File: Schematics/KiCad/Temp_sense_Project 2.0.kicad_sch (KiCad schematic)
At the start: 0 parts

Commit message: Fix all errors and warnings
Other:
- sheet Power renamed Power and Isolation
- sheet mux side left renamed Multiplexers
- sheet MCU ports: added CAN RX, CAN TX, Fault Line 1; removed 5V GND, 5V PWR, Fault line 1, RXD, TXD
- sheet Power and Isolation ports: added none; removed 5V GND, 5V PWR
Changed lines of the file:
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@@
-	(wire
-		(pts
-			(xy 416.56 278.13) (xy 416.56 266.7)
-		)
-		(stroke
-			(width 0)
-			(type default)
-		)
-	)
 	(wire
 		(pts
@@
 		(pts
 			(xy 424.18 219.71) (xy 419.1 219.71)
-		)
-		(stroke
-			(width 0)
-			(type default)
-		)
-	)
-	(wire
-		(pts
-			(xy 419.1 278.13) (xy 419.1 266.7)
 		)
 		(stroke
@@
 			(color 128 255 128 1.0000)
 		)
-		(property "Sheetname" "mux side left"
+		(property "Sheetname" "Multiplexers"
 			(at 384.81 207.01 0)
 			(effects
@@
 			)
 		)
-		(pin "5V GND" input
-			(at 416.56 266.7 270)
-			(effects
-				(font
-					(size 1.27 1.27)
-				)
-				(justify left)
-			)
-		)
-		(pin "5V PWR" input
-			(at 419.1 266.7 270)
-			(effects
-				(font
-					(size 1.27 1.27)
-				)
-				(justify left)
-			)
-		)
-		(pin "TXD" output
+		(pin "Fault Line 1" output
+			(at 425.45 266.7 270)
+			(effects
+				(font
+					(size 1.27 1.27)
+				)
+				(justify left)
+			)
+		)
+		(pin "CAN RX" input
+			(at 378.46 266.7 270)
+			(effects
+				(font
+					(size 1.27 1.27)
+				)
+				(justify left)
+			)
+		)
+		(pin "CAN TX" output
 			(at 383.54 266.7 270)
-			(effects
-				(font
-					(size 1.27 1.27)
-				)
-				(justify left)
-			)
-		)
-		(pin "RXD" input
-			(at 378.46 266.7 270)
-			(effects
-				(font
-					(size 1.27 1.27)
-				)
-				(justify left)
-			)
-		)
-		(pin "Fault line 1" output
-			(at 425.45 266.7 270)
 			(effects
 				(font
@@
 			(color 128 255 128 1.0000)
 		)
-		(property "Sheetname" "Power"
+		(property "Sheetname" "Power and Isolation"
 			(at 371.3984 298.45 90)
 			(effects
@@
 			)
 		)
-		(pin "5V GND" output
-			(at 416.56 278.13 90)
-			(effects
-				(font
-					(size 1.27 1.27)
-				)
-				(justify right)
-			)
-		)
-		(pin "5V PWR" output
-			(at 419.1 278.13 90)
-			(effects
-				(font
-					(size 1.27 1.27)
-				)
-				(justify right)
-			)
-		)

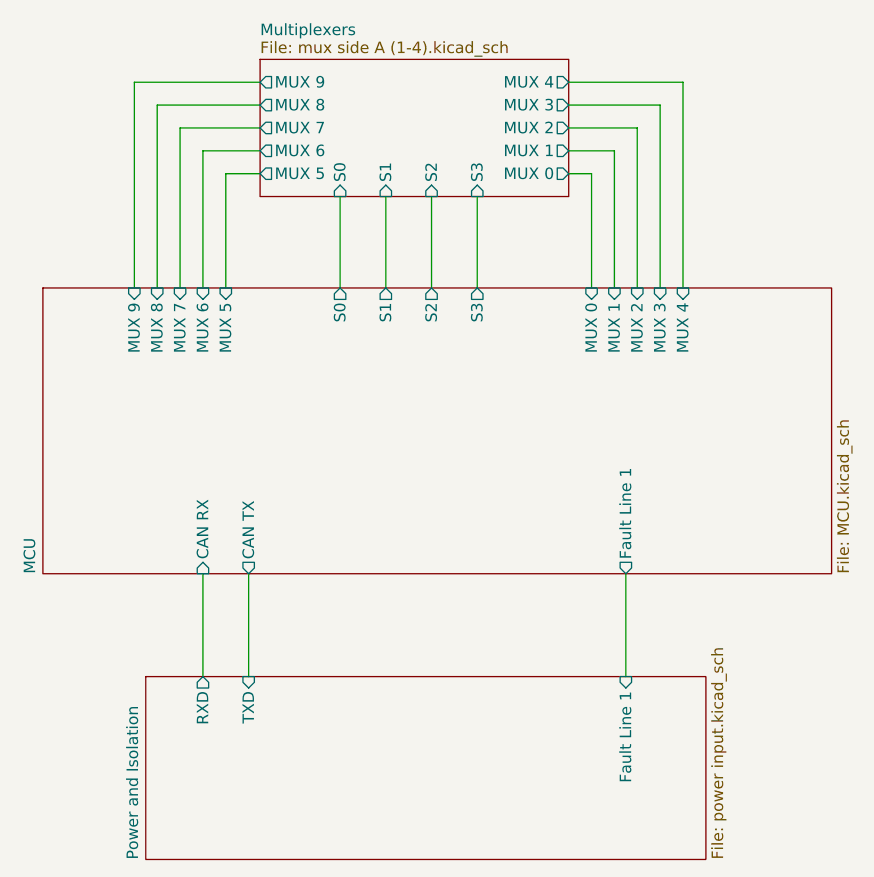
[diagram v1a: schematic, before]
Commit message: Condense layout to 2 layers
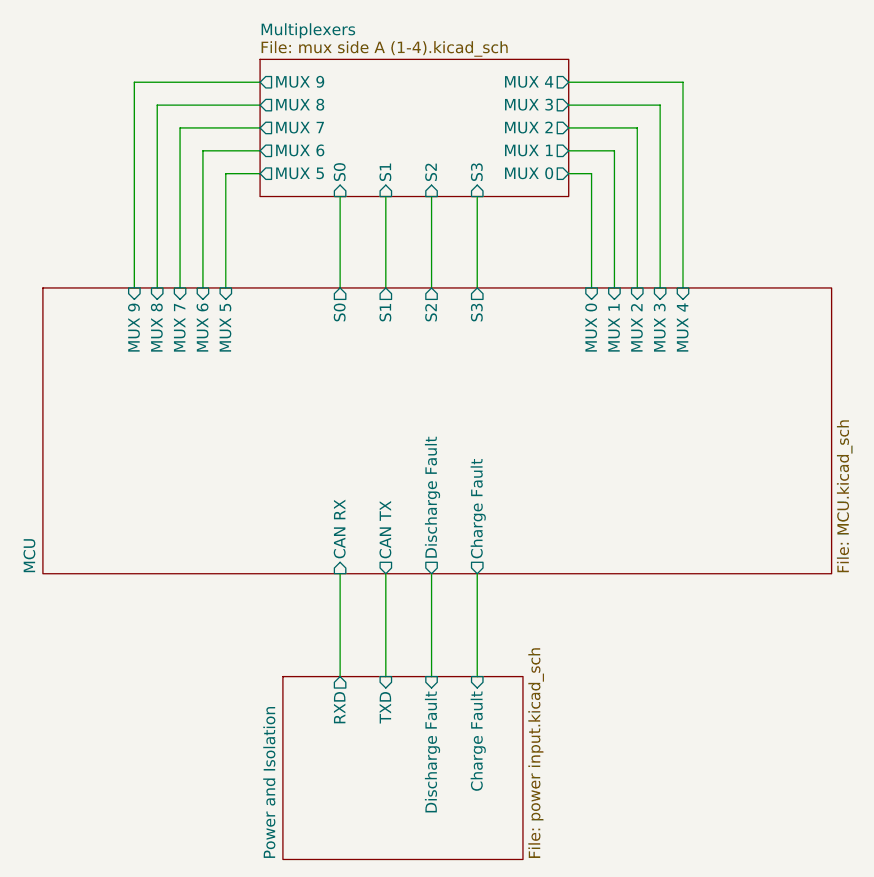
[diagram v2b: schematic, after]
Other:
- sheet MCU ports: added Charge Fault, Discharge Fault; removed Fault Line 1
- sheet Power and Isolation ports: added Charge Fault, Discharge Fault; removed Fault Line 1
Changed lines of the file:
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@@
 	(wire
 		(pts
-			(xy 383.54 278.13) (xy 383.54 266.7)
+			(xy 398.78 278.13) (xy 398.78 266.7)
 		)
 		(stroke
@@
 	(wire
 		(pts
-			(xy 425.45 266.7) (xy 425.45 278.13)
+			(xy 408.94 266.7) (xy 408.94 278.13)
 		)
 		(stroke
@@
 	(wire
 		(pts
+			(xy 403.86 278.13) (xy 403.86 266.7)
+		)
+		(stroke
+			(width 0)
+			(type default)
+		)
+	)
+	(wire
+		(pts
 			(xy 370.84 212.09) (xy 370.84 234.95)
 		)
@@
 	(wire
 		(pts
-			(xy 378.46 278.13) (xy 378.46 266.7)
+			(xy 393.7 278.13) (xy 393.7 266.7)
 		)
 		(stroke
@@
 			)
 		)
-		(pin "Fault Line 1" output
-			(at 425.45 266.7 270)
-			(effects
-				(font
-					(size 1.27 1.27)
-				)
-				(justify left)
-			)
-		)
 		(pin "CAN RX" input
-			(at 378.46 266.7 270)
+			(at 393.7 266.7 270)
 			(effects
 				(font
@@
 		)
 		(pin "CAN TX" output
-			(at 383.54 266.7 270)
+			(at 398.78 266.7 270)
+			(effects
+				(font
+					(size 1.27 1.27)
+				)
+				(justify left)
+			)
+		)
+		(pin "Charge Fault" output
+			(at 408.94 266.7 270)
+			(effects
+				(font
+					(size 1.27 1.27)
+				)
+				(justify left)
+			)
+		)
+		(pin "Discharge Fault" output
+			(at 403.86 266.7 270)
 			(effects
 				(font
@@
 	)
 	(sheet
-		(at 372.11 278.13)
-		(size 62.23 20.32)
+		(at 387.35 278.13)
+		(size 26.67 20.32)
 		(exclude_from_sim no)
 		(in_bom yes)
@@
 		)
 		(property "Sheetname" "Power and Isolation"
-			(at 371.3984 298.45 90)
+			(at 386.6384 298.45 90)
 			(effects
 				(font
@@
 		)
 		(property "Sheetfile" "power input.kicad_sch"
-			(at 434.9246 298.45 90)
+			(at 414.6046 298.45 90)
 			(effects
 				(font
@@
 			)
 		)
-		(pin "Fault Line 1" input
-			(at 425.45 278.13 90)
-			(effects
-				(font
-					(size 1.27 1.27)
-				)
-				(justify right)
-			)
-		)
 		(pin "RXD" output
-			(at 378.46 278.13 90)
+			(at 393.7 278.13 90)
 			(effects
 				(font
@@
 		)
 		(pin "TXD" input
-			(at 383.54 278.13 90)
-			(effects
-				(font
+			(at 398.78 278.13 90)
+			(effects
+				(font
+					(size 1.27 1.27)
+				)
+				(justify right)
+			)
+		)
+		(pin "Charge Fault" input
+			(at 408.94 278.13 90)
+			(effects
+				(font
+					(size 1.27 1.27)
+				)
+				(justify right)
+			)
+		)
+		(pin "Discharge Fault" input
+			(at 403.86 278.13 90)
+			(effects
+				(font
